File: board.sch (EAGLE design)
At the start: 85 parts, among them J1 AVR_SPI_PRG_6NS, U1 TPS2112A, U2 MAX1555, U3 USD-SOCKETNEW, U4 3.3V, U5 2.8V, U6 74HC595, Y1 8MHz, Y2 12.288MHz

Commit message: Switched audio plug to 3-pin version and added OE connection
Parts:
- U7: device SparkFun-Connectors:AUDIO-JACKSMD2 -> mkmp3:AUDIO-JACKSMD2
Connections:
- new net SHIFT_OE: U$1.PD6(RTS/AIN5/INT6), U6.OE
- net DS: now also U$1.PD7(CTS/HWB/AIN6/T0/INT7); no longer U$1.PD6(RTS/AIN5/INT6)
- net GND: no longer U6.OE
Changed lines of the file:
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@@
 <part name="SUPPLY29" library="supply2" deviceset="GND" device=""/>
 <part name="S2" library="mkmp3" deviceset="EVQ-WKA" device=""/>
-<part name="U7" library="SparkFun-Connectors" deviceset="AUDIO-JACK" device="SMD2"/>
+<part name="U7" library="mkmp3" deviceset="AUDIO-JACK" device="SMD2"/>
 <part name="LED8" library="LilyPad-Wearables" deviceset="LED" device="1206"/>
 <part name="LED7" library="LilyPad-Wearables" deviceset="LED" device="1206"/>
@@
 <part name="SUPPLY32" library="supply2" deviceset="GND" device=""/>
 <part name="SUPPLY33" library="supply2" deviceset="VDD" device=""/>
-<part name="SUPPLY34" library="supply2" deviceset="GND" device=""/>
 <part name="U4" library="mkmp3" deviceset="LM3671" device="" value="3.3V"/>
 <part name="U5" library="mkmp3" deviceset="LM3671" device="" value="2.8V"/>
@@
 <instance part="SUPPLY32" gate="GND" x="314.96" y="129.54"/>
 <instance part="SUPPLY33" gate="G$1" x="279.4" y="121.92" rot="R90"/>
-<instance part="SUPPLY34" gate="GND" x="287.02" y="121.92" rot="R90"/>
 <instance part="U4" gate="G$1" x="142.24" y="177.8"/>
 <instance part="U5" gate="G$1" x="142.24" y="154.94"/>
@@
 </segment>
 <segment>
-<pinref part="U6" gate="G$1" pin="OE"/>
-<pinref part="SUPPLY34" gate="GND" pin="GND"/>
-</segment>
-<segment>
 <pinref part="C9" gate="G$1" pin="2"/>
 <pinref part="U5" gate="G$1" pin="GND"/>
@@
 </segment>
 <segment>
-<label x="83.82" y="45.72" size="1.778" layer="95"/>
-<pinref part="U$1" gate="G$1" pin="PD6(RTS/AIN5/INT6)"/>
-<wire x1="78.74" y1="45.72" x2="88.9" y2="45.72" width="0.1524" layer="91"/>
+<pinref part="U$1" gate="G$1" pin="PD7(CTS/HWB/AIN6/T0/INT7)"/>
+<wire x1="78.74" y1="43.18" x2="88.9" y2="43.18" width="0.1524" layer="91"/>
+<label x="83.82" y="43.18" size="1.778" layer="95"/>
 </segment>
 </net>
@@
 </segment>
 </net>
+<net name="SHIFT_OE" class="0">
+<segment>
+<pinref part="U6" gate="G$1" pin="OE"/>
+<wire x1="284.48" y1="121.92" x2="284.48" y2="114.3" width="0.1524" layer="91"/>
+<label x="284.48" y="114.3" size="1.778" layer="95"/>
+</segment>
+<segment>
+<label x="83.82" y="45.72" size="1.778" layer="95"/>
+<pinref part="U$1" gate="G$1" pin="PD6(RTS/AIN5/INT6)"/>
+<wire x1="78.74" y1="45.72" x2="88.9" y2="45.72" width="0.1524" layer="91"/>
+</segment>
+</net>

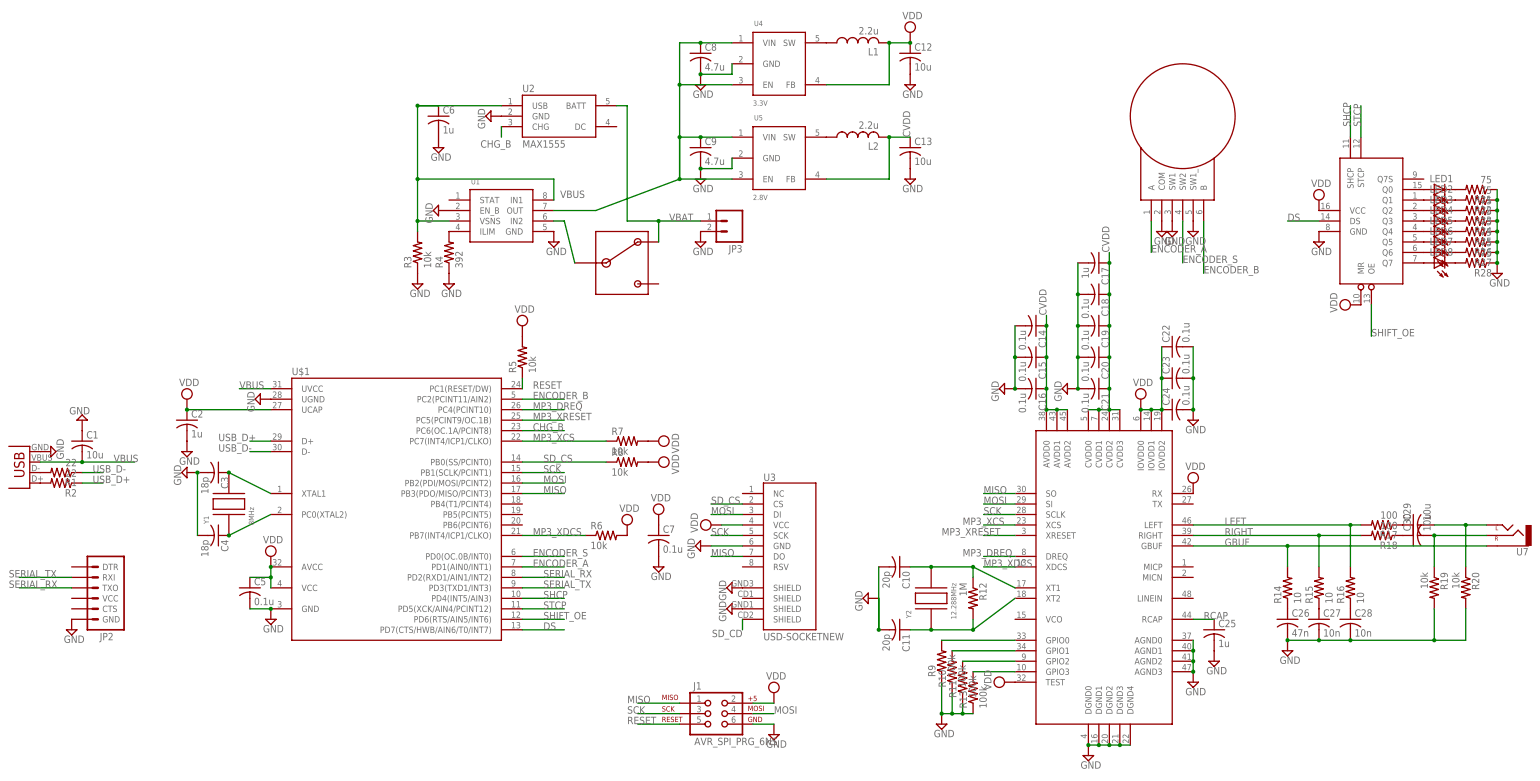
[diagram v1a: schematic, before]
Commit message: Fixed rear silkscreen
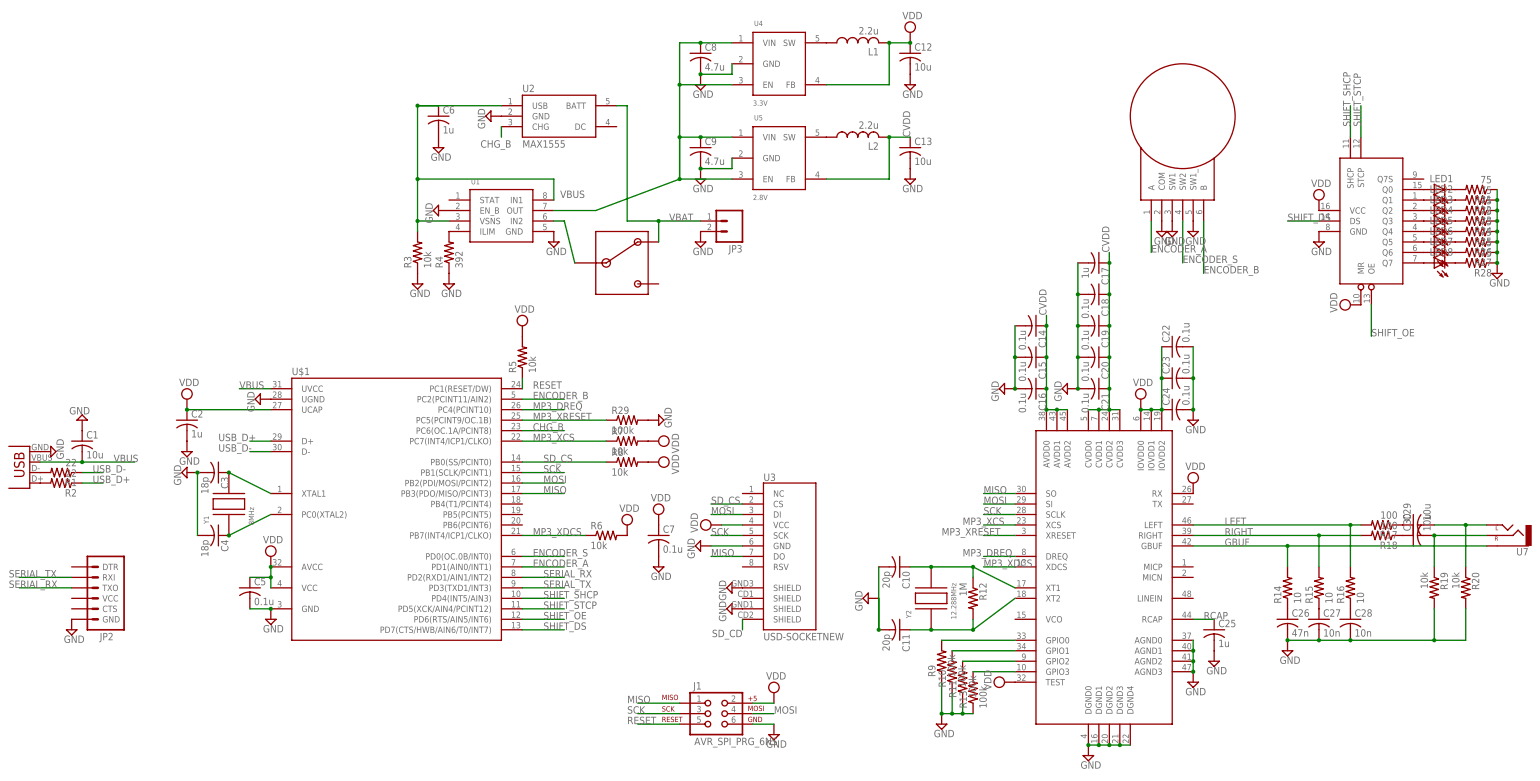
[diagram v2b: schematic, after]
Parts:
- added R29: 100k, rcl:R-US_R0603W
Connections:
- net DS renamed SHIFT_DS
- net SHCP renamed SHIFT_SHCP
- net STCP renamed SHIFT_STCP
- net GND: now also R29.2
- net MP3_XRESET: now also R29.1
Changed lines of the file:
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@@
 <part name="SUPPLY19" library="supply2" deviceset="VDD" device=""/>
 <part name="SUPPLY52" library="supply2" deviceset="VDD" device=""/>
+<part name="R29" library="rcl" deviceset="R-US_" device="R0603W" value="100k"/>
+<part name="SUPPLY34" library="supply2" deviceset="GND" device=""/>
 </parts>
 <sheets>
@@
 <instance part="SUPPLY19" gate="G$1" x="111.76" y="88.9" rot="R270"/>
 <instance part="SUPPLY52" gate="G$1" x="111.76" y="83.82" rot="R270"/>
+<instance part="R29" gate="G$1" x="104.14" y="93.98"/>
+<instance part="SUPPLY34" gate="GND" x="111.76" y="93.98" rot="R90"/>
 </instances>
 <busses>
@@
 <pinref part="SUPPLY10" gate="GND" pin="GND"/>
 <junction x="180.34" y="22.86"/>
+</segment>
+<segment>
+<pinref part="R29" gate="G$1" pin="2"/>
+<pinref part="SUPPLY34" gate="GND" pin="GND"/>
 </segment>
 </net>
@@
 <label x="81.28" y="93.98" size="1.778" layer="95"/>
 <pinref part="U$1" gate="G$1" pin="PC5(PCINT9/OC.1B)"/>
-<wire x1="78.74" y1="93.98" x2="88.9" y2="93.98" width="0.1524" layer="91"/>
+<wire x1="78.74" y1="93.98" x2="99.06" y2="93.98" width="0.1524" layer="91"/>
+<pinref part="R29" gate="G$1" pin="1"/>
 </segment>
 </net>
@@
 </segment>
 </net>
-<net name="SHCP" class="0">
+<net name="SHIFT_SHCP" class="0">
 <segment>
 <pinref part="U6" gate="G$1" pin="SHCP"/>
@@
 </segment>
 </net>
-<net name="STCP" class="0">
+<net name="SHIFT_STCP" class="0">
 <segment>
 <pinref part="U6" gate="G$1" pin="STCP"/>
@@
 </segment>
 </net>
-<net name="DS" class="0">
+<net name="SHIFT_DS" class="0">
 <segment>
 <pinref part="U6" gate="G$1" pin="DS"/>

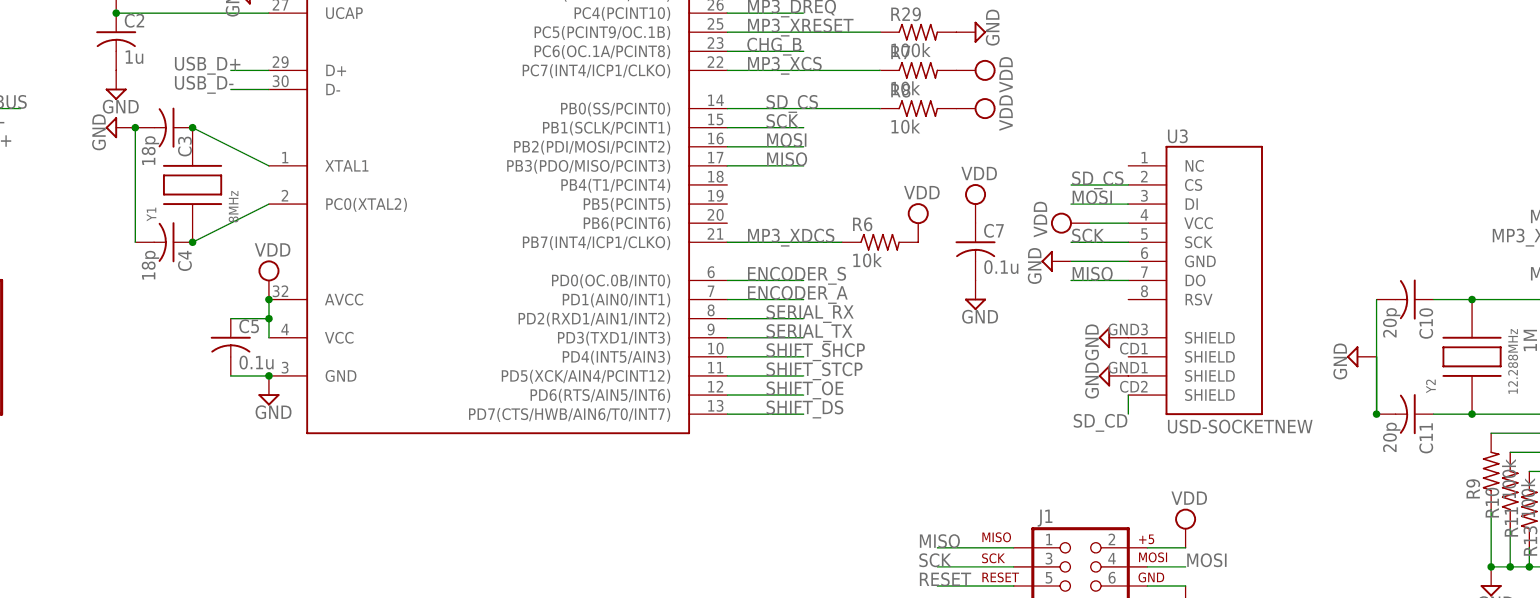
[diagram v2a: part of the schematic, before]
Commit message: Capacitor value fixes and obsessive pcb trace cleanup
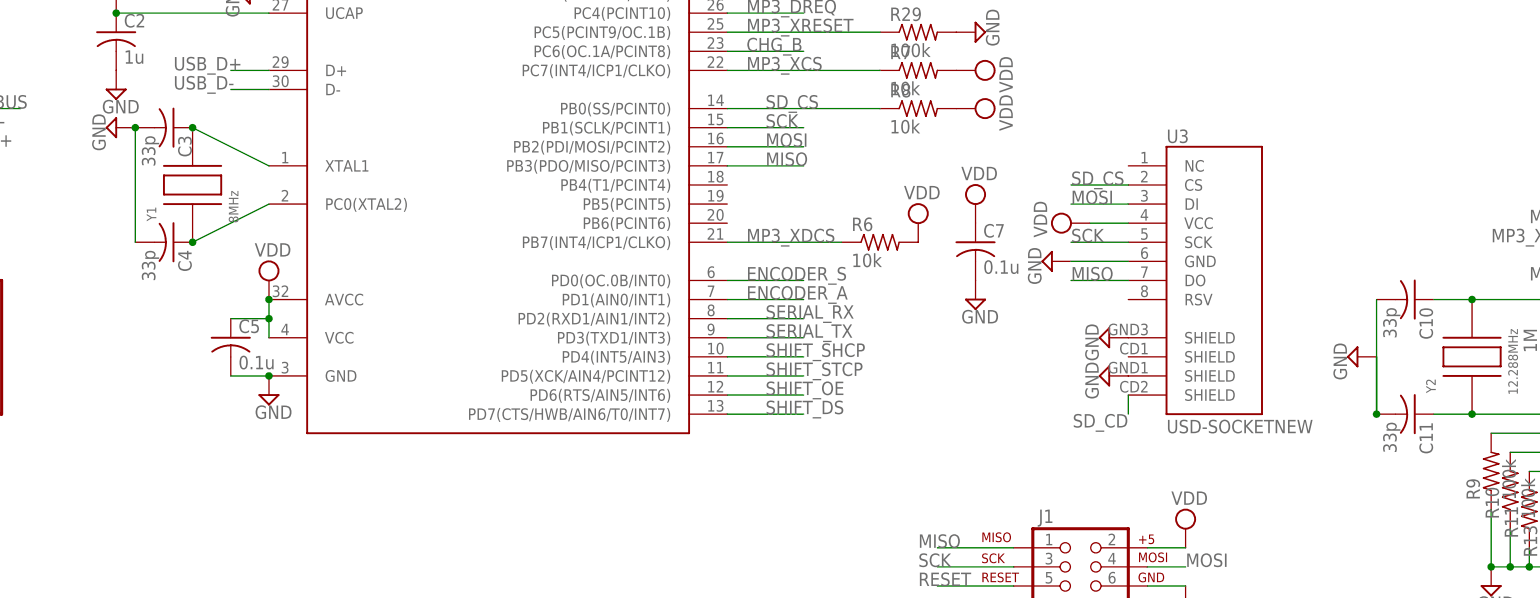
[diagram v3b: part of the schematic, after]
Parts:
- C10, C11: value 20p -> 33p
- C3, C4: value 18p -> 33p
- R1, R2, R8: device rcl:R-US_R0603 -> rcl:R-US_R0603W
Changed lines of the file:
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@@
 <grid distance="0.1" unitdist="inch" unit="inch" style="lines" multiple="1" display="no" altdistance="0.01" altunitdist="inch" altunit="inch"/>
 <layers>
-<layer number="1" name="Top" color="4" fill="1" visible="no" active="no"/>
-<layer number="16" name="Bottom" color="1" fill="1" visible="no" active="no"/>
-<layer number="17" name="Pads" color="2" fill="1" visible="no" active="no"/>
-<layer number="18" name="Vias" color="2" fill="1" visible="no" active="no"/>
-<layer number="19" name="Unrouted" color="6" fill="1" visible="no" active="no"/>
-<layer number="20" name="Dimension" color="15" fill="1" visible="no" active="no"/>
-<layer number="21" name="tPlace" color="14" fill="1" visible="no" active="no"/>
-<layer number="22" name="bPlace" color="7" fill="1" visible="no" active="no"/>
-<layer number="23" name="tOrigins" color="15" fill="1" visible="no" active="no"/>
-<layer number="24" name="bOrigins" color="15" fill="1" visible="no" active="no"/>
-<layer number="25" name="tNames" color="7" fill="1" visible="no" active="no"/>
-<layer number="26" name="bNames" color="7" fill="1" visible="no" active="no"/>
-<layer number="27" name="tValues" color="7" fill="1" visible="no" active="no"/>
-<layer number="28" name="bValues" color="7" fill="1" visible="no" active="no"/>
+<layer number="1" name="Top" color="4" fill="1" visible="yes" active="no"/>
+<layer number="16" name="Bottom" color="1" fill="1" visible="yes" active="no"/>
+<layer number="17" name="Pads" color="2" fill="1" visible="yes" active="no"/>
+<layer number="18" name="Vias" color="2" fill="1" visible="yes" active="no"/>
+<layer number="19" name="Unrouted" color="6" fill="1" visible="yes" active="no"/>
+<layer number="20" name="Dimension" color="15" fill="1" visible="yes" active="no"/>
+<layer number="21" name="tPlace" color="14" fill="1" visible="yes" active="no"/>
+<layer number="22" name="bPlace" color="7" fill="1" visible="yes" active="no"/>
+<layer number="23" name="tOrigins" color="15" fill="1" visible="yes" active="no"/>
+<layer number="24" name="bOrigins" color="15" fill="1" visible="yes" active="no"/>
+<layer number="25" name="tNames" color="7" fill="1" visible="yes" active="no"/>
+<layer number="26" name="bNames" color="7" fill="1" visible="yes" active="no"/>
+<layer number="27" name="tValues" color="7" fill="1" visible="yes" active="no"/>
+<layer number="28" name="bValues" color="7" fill="1" visible="yes" active="no"/>
 <layer number="29" name="tStop" color="7" fill="3" visible="no" active="no"/>
 <layer number="30" name="bStop" color="7" fill="6" visible="no" active="no"/>
@@
 <layer number="35" name="tGlue" color="7" fill="4" visible="no" active="no"/>
 <layer number="36" name="bGlue" color="7" fill="5" visible="no" active="no"/>
-<layer number="37" name="tTest" color="7" fill="1" visible="no" active="no"/>
-<layer number="38" name="bTest" color="7" fill="1" visible="no" active="no"/>
+<layer number="37" name="tTest" color="7" fill="1" visible="yes" active="no"/>
+<layer number="38" name="bTest" color="7" fill="1" visible="yes" active="no"/>
 <layer number="39" name="tKeepout" color="4" fill="11" visible="no" active="no"/>
 <layer number="40" name="bKeepout" color="1" fill="11" visible="no" active="no"/>
@@
 <layer number="44" name="Drills" color="7" fill="1" visible="no" active="no"/>
 <layer number="45" name="Holes" color="7" fill="1" visible="no" active="no"/>
-<layer number="46" name="Milling" color="3" fill="1" visible="no" active="no"/>
-<layer number="47" name="Measures" color="7" fill="1" visible="no" active="no"/>
-<layer number="48" name="Document" color="7" fill="1" visible="no" active="no"/>
-<layer number="49" name="Reference" color="7" fill="1" visible="no" active="no"/>
-<layer number="50" name="dxf" color="7" fill="1" visible="no" active="no"/>
-<layer number="51" name="tDocu" color="7" fill="1" visible="no" active="no"/>
-<layer number="52" name="bDocu" color="7" fill="1" visible="no" active="no"/>
-<layer number="53" name="tGND_GNDA" color="7" fill="9" visible="no" active="no"/>
-<layer number="54" name="bGND_GNDA" color="1" fill="9" visible="no" active="no"/>
-<layer number="56" name="wert" color="7" fill="1" visible="no" active="no"/>
+<layer number="46" name="Milling" color="3" fill="1" visible="yes" active="no"/>
+<layer number="47" name="Measures" color="7" fill="1" visible="yes" active="no"/>
+<layer number="48" name="Document" color="7" fill="1" visible="yes" active="no"/>
+<layer number="49" name="Reference" color="7" fill="1" visible="yes" active="no"/>
+<layer number="50" name="dxf" color="7" fill="1" visible="yes" active="no"/>
+<layer number="51" name="tDocu" color="7" fill="1" visible="yes" active="no"/>
+<layer number="52" name="bDocu" color="7" fill="1" visible="yes" active="no"/>
+<layer number="53" name="tGND_GNDA" color="7" fill="9" visible="yes" active="no"/>
+<layer number="54" name="bGND_GNDA" color="1" fill="9" visible="yes" active="no"/>
+<layer number="56" name="wert" color="7" fill="1" visible="yes" active="no"/>
 <layer number="91" name="Nets" color="2" fill="1" visible="yes" active="yes"/>
 <layer number="92" name="Busses" color="1" fill="1" visible="yes" active="yes"/>
@@
 <part name="SUPPLY11" library="supply2" deviceset="GND" device=""/>
 <part name="SUPPLY9" library="supply2" deviceset="GND" device=""/>
-<part name="R1" library="rcl" deviceset="R-US_" device="R0603" value="22"/>
-<part name="R2" library="rcl" deviceset="R-US_" device="R0603" value="22"/>
+<part name="R1" library="rcl" deviceset="R-US_" device="R0603W" value="22"/>
+<part name="R2" library="rcl" deviceset="R-US_" device="R0603W" value="22"/>
 <part name="C2" library="rcl" deviceset="C-US" device="C0603K" value="1u"/>
 <part name="SUPPLY12" library="supply2" deviceset="GND" device=""/>
@@
 <part name="SUPPLY16" library="supply2" deviceset="GND" device=""/>
 <part name="Y2" library="mkmp3" deviceset="CSM-3X" device="" value="12.288MHz"/>
-<part name="C10" library="rcl" deviceset="C-US" device="C0603K" value="20p"/>
-<part name="C11" library="rcl" deviceset="C-US" device="C0603K" value="20p"/>
+<part name="C10" library="rcl" deviceset="C-US" device="C0603K" value="33p"/>
+<part name="C11" library="rcl" deviceset="C-US" device="C0603K" value="33p"/>
 <part name="SUPPLY17" library="supply2" deviceset="GND" device=""/>
 <part name="Y1" library="mkmp3" deviceset="CSM-7X" device="" value="8MHz"/>
-<part name="C3" library="rcl" deviceset="C-US" device="C0603K" value="18p"/>
-<part name="C4" library="rcl" deviceset="C-US" device="C0603K" value="18p"/>
+<part name="C3" library="rcl" deviceset="C-US" device="C0603K" value="33p"/>
+<part name="C4" library="rcl" deviceset="C-US" device="C0603K" value="33p"/>
 <part name="SUPPLY18" library="supply2" deviceset="GND" device=""/>
 <part name="SUPPLY20" library="supply2" deviceset="VDD" device=""/>
@@
 <part name="SUPPLY10" library="supply2" deviceset="GND" device=""/>
 <part name="R7" library="rcl" deviceset="R-US_" device="R0603W" value="10k"/>
-<part name="R8" library="rcl" deviceset="R-US_" device="R0603" value="10k"/>
+<part name="R8" library="rcl" deviceset="R-US_" device="R0603W" value="10k"/>
 <part name="R6" library="rcl" deviceset="R-US_" device="R0603W" value="10k"/>
 <part name="SUPPLY14" library="supply2" deviceset="VDD" device=""/>
